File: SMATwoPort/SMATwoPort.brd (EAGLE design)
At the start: 20.1 x 15.2 mm, 3 parts

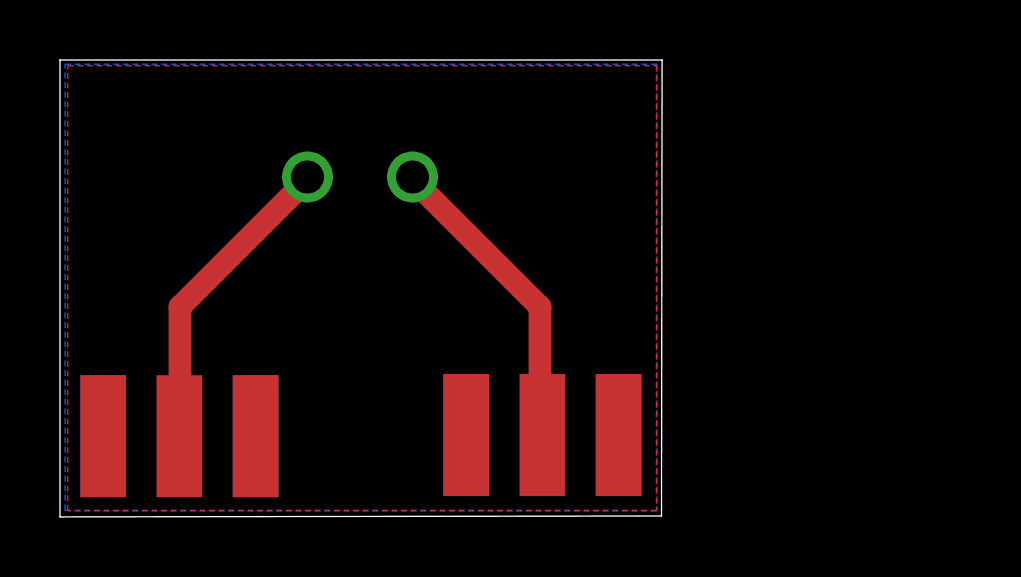
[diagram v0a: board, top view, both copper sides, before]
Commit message: Updated pcb to have sma's on the side to accommodate Network Analyzer cables.
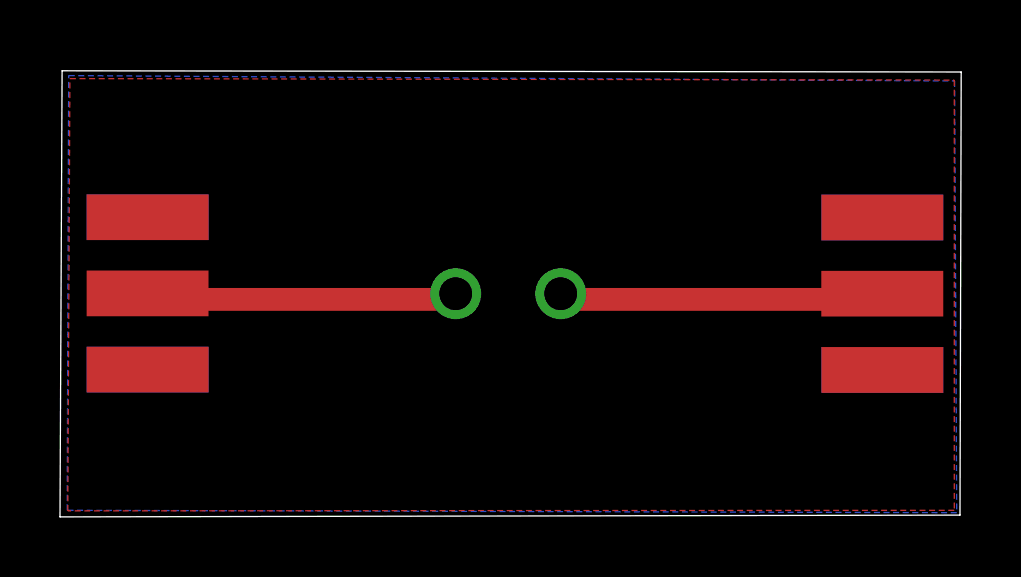
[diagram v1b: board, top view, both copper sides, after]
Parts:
- moved J$2 14.0 mm to (27.4, 4.90), turned to 90 degrees
- moved J$1 7.45 mm to (2.92, 9.99), turned to 270 degrees
- moved PORT 6.29 mm to (14.9, 7.54)
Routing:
- net N$1: track 10.4 -> 10.9 mm
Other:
- board size 20.1 x 15.2 mm -> 30 x 14.9 mm
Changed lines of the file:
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@@
 <?xml version="1.0" encoding="utf-8"?>
 <!DOCTYPE eagle SYSTEM "eagle.dtd">
-<eagle version="7.4.0">
+<eagle version="7.2.0">
 <drawing>
 <settings>
@@
 <board>
 <plain>
-<wire x1="0" y1="0" x2="20.05" y2="0.03" width="0" layer="20"/>
-<wire x1="20.05" y1="0.03" x2="20.07" y2="15.23" width="0" layer="20"/>
-<wire x1="20.07" y1="15.23" x2="0" y2="15.23" width="0" layer="20"/>
-<wire x1="0" y1="15.23" x2="0" y2="0" width="0" layer="20"/>
-<dimension x1="0.05" y1="-4.89" x2="20.05" y2="-6.94" x3="10.05" y3="-2.94" textsize="1.778" layer="21" dtype="horizontal"/>
+<wire x1="0" y1="0" x2="30" y2="0.06" width="0" layer="20"/>
+<wire x1="30" y1="0.06" x2="30.04" y2="14.83" width="0" layer="20"/>
+<wire x1="30.04" y1="14.83" x2="0.07" y2="14.87" width="0" layer="20"/>
+<wire x1="0.07" y1="14.87" x2="0" y2="0" width="0" layer="20"/>
+<dimension x1="0.05" y1="-4.89" x2="30.06" y2="-6.83" x3="15.055" y3="-2.94" textsize="1.778" layer="21" dtype="horizontal"/>
+<dimension x1="0.07" y1="14.87" x2="0" y2="0" x3="-3.16" y3="7.435" textsize="1.778" layer="21" dtype="vertical"/>
 </plain>
 <attributes>
@@
 </autorouter>
 <elements>
-<element name="J$1" library="sparkfun-connectors" package="SMA-EDGE" value="SMA_EDGE" x="1.44" y="2.69"/>
-<element name="J$2" library="sparkfun-connectors" package="SMA-EDGE" value="SMA_EDGE" x="13.54" y="2.73"/>
-<element name="PORT" library="con-phoenix-350" package="1751248" value="1751248" x="10" y="11.43" rot="MR0">
-<attribute name="OC_NEWARK" value="unknown" x="10" y="11.43" size="1.778" layer="28" rot="MR0" display="off"/>
-<attribute name="MPN" value="" x="10" y="11.43" size="1.778" layer="28" rot="MR0" display="off"/>
-<attribute name="MF" value="" x="10" y="11.43" size="1.778" layer="28" rot="MR0" display="off"/>
-<attribute name="OC_FARNELL" value="unknown" x="10" y="11.43" size="1.778" layer="28" rot="MR0" display="off"/>
+<element name="J$1" library="sparkfun-connectors" package="SMA-EDGE" value="SMA_EDGE" x="2.92" y="9.99" rot="R270"/>
+<element name="J$2" library="sparkfun-connectors" package="SMA-EDGE" value="SMA_EDGE" x="27.41" y="4.9" rot="R90"/>
+<element name="PORT" library="con-phoenix-350" package="1751248" value="1751248" x="14.94" y="7.54" rot="MR0">
+<attribute name="OC_NEWARK" value="unknown" x="14.94" y="7.54" size="1.778" layer="28" rot="MR0" display="off"/>
+<attribute name="MPN" value="" x="14.94" y="7.54" size="1.778" layer="28" rot="MR0" display="off"/>
+<attribute name="MF" value="" x="14.94" y="7.54" size="1.778" layer="28" rot="MR0" display="off"/>
+<attribute name="OC_FARNELL" value="unknown" x="14.94" y="7.54" size="1.778" layer="28" rot="MR0" display="off"/>
 </element>
 </elements>
 <signals>
-<signal name="N$3">
-<contactref element="J$1" pad="SIG"/>
-<contactref element="PORT" pad="2"/>
-<wire x1="4" y1="7" x2="8.25" y2="11.25" width="0.762" layer="1"/>
-<wire x1="4" y1="2.75" x2="4" y2="7" width="0.762" layer="1"/>
-<wire x1="8.25" y1="11.25" x2="8.25" y2="11.33" width="0.762" layer="1"/>
-<wire x1="4" y1="2.75" x2="3.98" y2="2.69" width="0.762" layer="1"/>
-</signal>
-<signal name="N$4">
-<contactref element="J$2" pad="SIG"/>
-<contactref element="PORT" pad="1"/>
-<wire x1="16" y1="7" x2="11.75" y2="11.25" width="0.762" layer="1"/>
-<wire x1="16" y1="2.75" x2="16" y2="7" width="0.762" layer="1"/>
-<wire x1="11.75" y1="11.25" x2="11.75" y2="11.33" width="0.762" layer="1"/>
-<wire x1="16" y1="2.75" x2="16.08" y2="2.73" width="0.762" layer="1"/>
-</signal>
 <signal name="GND">
 <polygon width="0.254" layer="16">
-<vertex x="0.17" y="15.09"/>
-<vertex x="19.9" y="15.09"/>
-<vertex x="19.9" y="0.22"/>
-<vertex x="0.17" y="0.22"/>
+<vertex x="0.29" y="14.71"/>
+<vertex x="29.82" y="14.53"/>
+<vertex x="29.89" y="0.14"/>
+<vertex x="0.24" y="0.22"/>
 </polygon>
 <polygon width="0.254" layer="1" spacing="1.6764">
-<vertex x="0.26" y="15.04"/>
-<vertex x="19.88" y="15.04"/>
-<vertex x="19.88" y="0.2"/>
+<vertex x="0.33" y="14.61"/>
+<vertex x="29.81" y="14.56"/>
+<vertex x="29.81" y="0.22"/>
 <vertex x="0.26" y="0.2"/>
 </polygon>
@@
 <contactref element="J$1" pad="GND@2"/>
 <contactref element="J$1" pad="GND@3"/>
-<wire x1="1.44" y1="2.69" x2="1.44" y2="2.69" width="0" layer="19" extent="1-16"/>
+<wire x1="2.92" y1="4.91" x2="2.92" y2="4.91" width="0" layer="19" extent="1-16"/>
+</signal>
+<signal name="N$1">
+<contactref element="J$2" pad="SIG"/>
+<contactref element="PORT" pad="1"/>
+<wire x1="27.25" y1="7.25" x2="16.75" y2="7.25" width="0.762" layer="1"/>
+<wire x1="16.75" y1="7.25" x2="16.69" y2="7.44" width="0.762" layer="1"/>
+<wire x1="27.25" y1="7.25" x2="27.41" y2="7.44" width="0.762" layer="1"/>
+</signal>
+<signal name="N$2">
+<contactref element="J$1" pad="SIG"/>
+<contactref element="PORT" pad="2"/>
+<wire x1="3" y1="7.25" x2="13" y2="7.25" width="0.762" layer="1"/>
+<wire x1="13" y1="7.25" x2="13.19" y2="7.44" width="0.762" layer="1"/>
+<wire x1="3" y1="7.25" x2="2.92" y2="7.45" width="0.762" layer="1"/>
 </signal>
 </signals>
